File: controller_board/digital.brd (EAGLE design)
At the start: 148 x 129.2 mm, 34 parts

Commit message: Pull commit
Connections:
- removed net ENABLE_GATE: U$81.4
- net EN_GATE: now also U$81.4
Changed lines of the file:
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@@
 <wire x1="53.0225" y1="3.81" x2="53.0225" y2="5.715" width="0.6096" layer="1"/>
 <wire x1="53.0225" y1="5.715" x2="53.0225" y2="10.795" width="0.6096" layer="16"/>
+<contactref element="U$81" pad="4"/>
+<wire x1="55.245" y1="13.0175" x2="40.6375" y2="33.3675" width="0" layer="19" extent="1-16"/>
 </signal>
 <signal name="ADC_M1">
@@
 <wire x1="9.2075" y1="34.29" x2="6.6675" y2="34.29" width="1.016" layer="16"/>
 </signal>
-<signal name="ENABLE_GATE">
-<contactref element="U$81" pad="4"/>
-</signal>
 <signal name="-15V">

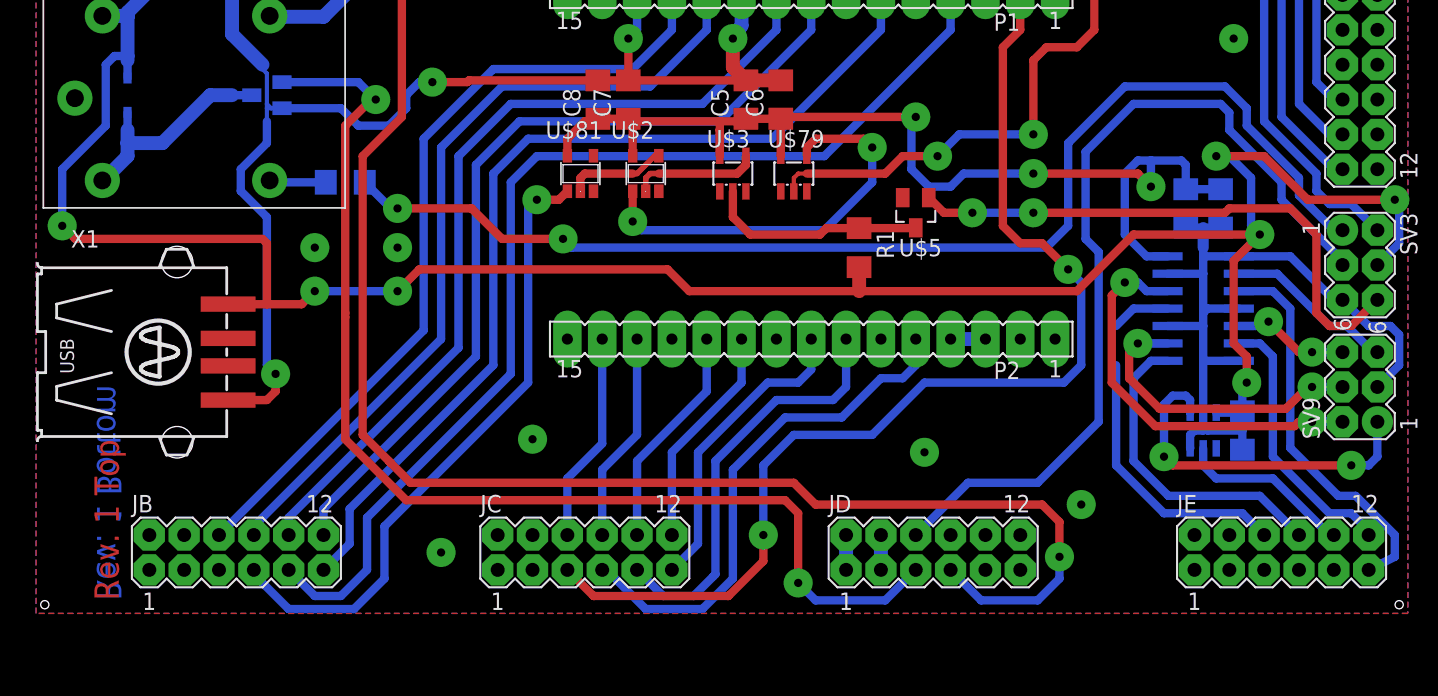
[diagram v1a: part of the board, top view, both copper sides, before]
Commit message: Added section of logic level shifters and drive enable signals!
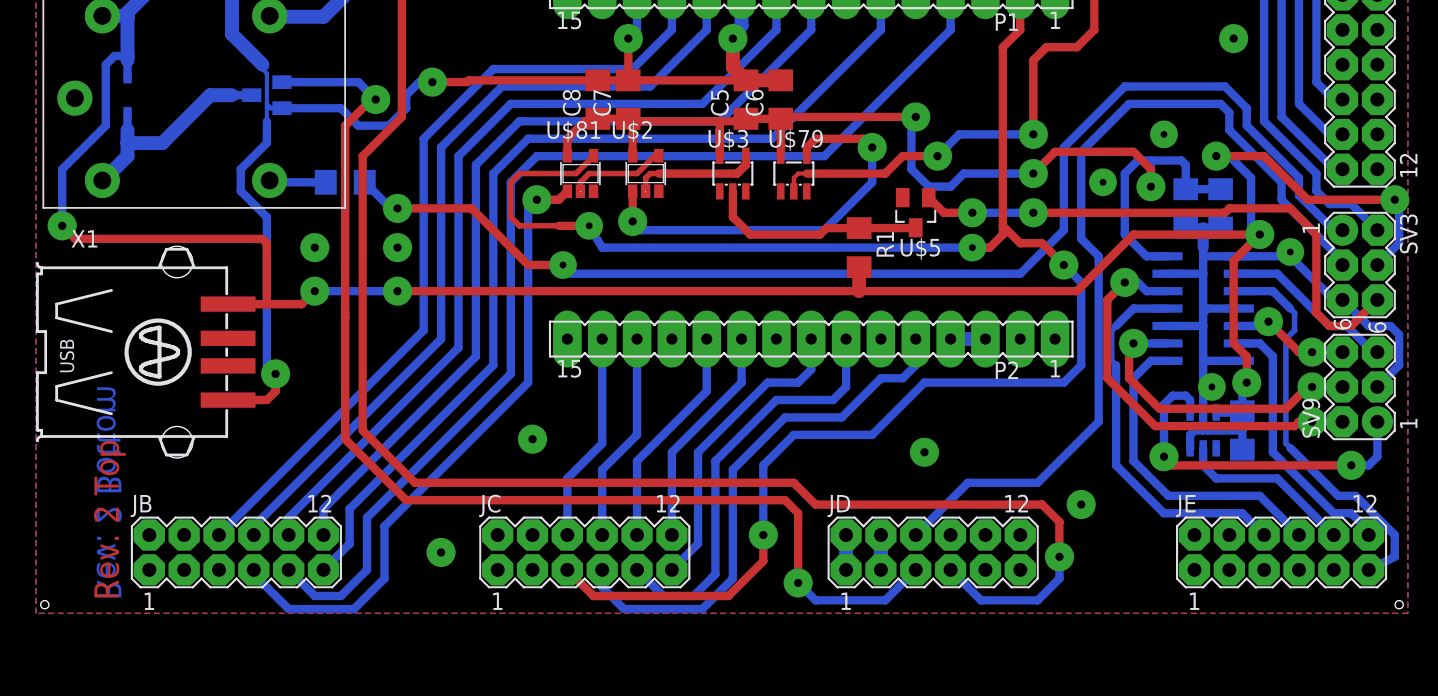
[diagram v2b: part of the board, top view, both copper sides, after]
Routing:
- net EN_GATE: track 80.4 -> 127.9 mm, vias 2 -> 4
- net +3V3: track 80.0 -> 82.0 mm
- net IR_RELAY: track 87.5 -> 89.1 mm
- net +5V: track 186.1 -> 184.8 mm
- net PWRGD: track 38.0 -> 38.7 mm
- net ZYBO_ENC_A: track 28.4 -> 28.9 mm
- net GNDD: vias 15 -> 19
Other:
- board text added: "Rev. 2 Bottom"
- board text added: "Rev. 2 Top"
- board text removed: "Rev. 1 Bottom"
- board text removed: "Rev. 1 Top"

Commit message: updates to boards
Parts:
- moved U$79 1.93 mm to (57.1, 32.4)
- moved R55 1.71 mm to (21.9, 33.0)
- moved U$3 0.71 mm to (51.1, 32.7)
- moved U$2 0.63 mm to (44.5, 32.7)
- moved U$81 0.63 mm to (39.7, 32.7)
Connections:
- removed net N$3: U$2.1, U$79.4
- removed net N$4: U$2.2, U$3.4
- new net ZYBO_OCP_EN_GATE: JB.5, U$2.1, U$79.4
- new net ZYBO_OTP_EN_GATE: JD.8, U$2.2, U$3.4
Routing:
- net GNDP: track 113.1 -> 7.79 mm
- net ZYBO_OCP_EN_GATE: track 0.00 -> 104.6 mm, vias 0 -> 5
- net ZYBO_OTP_EN_GATE: track 0.00 -> 69.2 mm, vias 0 -> 3
- net N$3: track 29.8 -> 0.00 mm, vias 2 -> 0
- net N$4: track 9.33 -> 0.00 mm
- net IR_RELAY: track 89.1 -> 92.1 mm
- net DRIVE_ENABLE: track 64.0 -> 66.8 mm
- net OCP_EN_GATE: track 66.6 -> 64.4 mm
- net ZYBO_IR_ENABLE: track 83.6 -> 85.4 mm
- net ZYBO_K1_ENABLE: track 121.6 -> 123.4 mm
- net ZYBO_EN_GATE: track 46.5 -> 47.5 mm
- net +3V3: track 82.0 -> 81.2 mm
- net EN_GATE: track 127.9 -> 128.8 mm
- net PWM2: track 59.7 -> 60.3 mm
- net GNDD: vias 19 -> 23
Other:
- board text added: "Rev. 3 Bottom"
- board text added: "Rev. 3 Top"
- board text removed: "Rev. 2 Bottom"
- board text removed: "Rev. 2 Top"

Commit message: Changes to Electronics Design
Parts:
- moved U$28 25.1 mm to (39.4, 54.0), flipped to the bottom, turned to 180 degrees
- moved U$46 11.4 mm to (13.0, 68.9), flipped to the bottom, turned to 180 degrees
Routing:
- net GNDD: track 200.3 -> 157.6 mm, vias 23 -> 22
- net GNDA: track 72.2 -> 32.4 mm
- net VBATT: track 92.4 -> 78.7 mm
- net +15V: track 21.9 -> 29.8 mm
- net -15V: track 29.1 -> 36.2 mm, vias 2 -> 1
- net +5V: track 185.1 -> 185.0 mm, vias 7 -> 8
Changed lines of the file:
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@@
 <attribute name="OC_NEWARK" value="unknown" x="96.52" y="16.51" size="1.778" layer="27" rot="R90" display="off"/>
 </element>
-<element name="U$28" library="custom_parts" package="TEN20-4823" value="TEN20-4823WIN" x="39.37" y="79.0575"/>
+<element name="U$28" library="custom_parts" package="TEN20-4823" value="TEN20-4823WIN" x="39.37" y="53.975" rot="MR180"/>
 <element name="U$36" library="custom_parts" package="SOT23-5L" value="SN74LVC1G17" x="85.09" y="13.335" rot="MR0"/>
-<element name="U$46" library="custom_parts" package="DIP24" value="TVN5-4811WI" x="13.0175" y="57.4675"/>
+<element name="U$46" library="custom_parts" package="DIP24" value="TVN5-4811WI" x="13.0175" y="68.8975" rot="MR180"/>
 <element name="U$49" library="custom_parts" package="JS1-5V-F" value="JS1-5V-F" x="11.43" y="37.465"/>
 <element name="U$55" library="custom_parts" package="MICROFIT-3.0" value="MICROFIT" x="29.21" y="76.835"/>
@@
 <wire x1="87.9475" y1="13.335" x2="85.4075" y2="13.335" width="0.6096" layer="16"/>
 <wire x1="85.4075" y1="13.335" x2="85.09" y2="13.6525" width="0.6096" layer="16"/>
-<wire x1="20.6375" y1="72.009" x2="17.7165" y2="72.009" width="1.016" layer="16"/>
-<wire x1="17.7165" y1="72.009" x2="16.51" y2="70.8025" width="1.016" layer="16"/>
-<wire x1="16.51" y1="70.8025" x2="16.51" y2="51.435" width="1.016" layer="16"/>
 <wire x1="15.5575" y1="46.355" x2="14.2875" y2="45.085" width="1.016" layer="16"/>
 <wire x1="14.2875" y1="45.085" x2="14.2875" y2="42.2275" width="1.016" layer="16"/>
@@
 <via x="66.675" y="13.0175" extent="1-16" drill="0.6"/>
 <contactref element="U$5" pad="2"/>
-<wire x1="5.3975" y1="51.816" x2="7.239" y2="51.816" width="1.016" layer="16"/>
-<wire x1="7.239" y1="51.816" x2="8.255" y2="51.7525" width="1.016" layer="16"/>
-<via x="8.255" y="51.7525" extent="1-16" drill="0.6"/>
-<wire x1="8.255" y1="51.7525" x2="13.0175" y2="51.7525" width="1.016" layer="1"/>
-<via x="13.0175" y="51.7525" extent="1-16" drill="0.6"/>
-<wire x1="13.0175" y1="51.7525" x2="16.1925" y2="51.7525" width="1.016" layer="16"/>
-<wire x1="16.1925" y1="51.7525" x2="16.51" y2="51.435" width="1.016" layer="16"/>
-<wire x1="16.51" y1="51.435" x2="16.51" y2="50.4825" width="1.016" layer="16"/>
-<wire x1="16.51" y1="50.4825" x2="17.78" y2="49.2125" width="1.016" layer="16"/>
-<wire x1="17.78" y1="49.2125" x2="20.574" y2="49.2125" width="1.016" layer="16"/>
-<wire x1="20.574" y1="49.2125" x2="20.6375" y2="49.149" width="1.016" layer="16"/>
 <wire x1="15.5575" y1="46.355" x2="19.685" y2="46.355" width="1.016" layer="16"/>
 <wire x1="19.685" y1="46.355" x2="20.6375" y2="47.3075" width="1.016" layer="16"/>
-<wire x1="20.6375" y1="47.3075" x2="20.6375" y2="49.149" width="1.016" layer="16"/>
 <wire x1="22.225" y1="36.83" x2="23.495" y2="35.56" width="0.6096" layer="16"/>
 <wire x1="23.495" y1="35.56" x2="25.7175" y2="35.56" width="0.6096" layer="16"/>
@@
 <via x="48.26" y="30.7975" extent="1-16" drill="0.6"/>
 <via x="54.2925" y="31.115" extent="1-16" drill="0.6"/>
+<via x="20.6375" y="47.3075" extent="1-16" drill="0.6"/>
+<wire x1="5.3975" y1="74.549" x2="20.6375" y2="77.216" width="0" layer="19" extent="1-1"/>
+<wire x1="20.6375" y1="54.356" x2="20.6375" y2="77.216" width="0" layer="19" extent="1-1"/>
 </signal>
 <signal name="ADC_M2">
@@
 <vertex x="87.3125" y="60.6425"/>
 </polygon>
-<wire x1="95.25" y1="67.6275" x2="82.55" y2="67.6275" width="1.016" layer="16"/>
-<wire x1="82.55" y1="67.6275" x2="76.2" y2="67.6275" width="1.016" layer="16"/>
-<wire x1="76.2" y1="67.6275" x2="74.93" y2="66.3575" width="1.016" layer="16"/>
-<wire x1="95.25" y1="75.2475" x2="84.7725" y2="75.2475" width="1.016" layer="16"/>
-<wire x1="84.7725" y1="75.2475" x2="82.55" y2="73.025" width="1.016" layer="16"/>
-<wire x1="82.55" y1="73.025" x2="82.55" y2="67.6275" width="1.016" layer="16"/>
 </signal>
 <signal name="VBATT">
@@
 <contactref element="U$46" pad="P$1"/>
 <contactref element="U$46" pad="P$2"/>
+<wire x1="38.735" y1="45.4025" x2="31.4325" y2="45.4025" width="1.016" layer="16"/>
 <wire x1="31.4325" y1="45.4025" x2="22.86" y2="45.4025" width="1.016" layer="16"/>
 <wire x1="22.86" y1="45.4025" x2="20.955" y2="43.4975" width="1.016" layer="16"/>
 <wire x1="20.955" y1="43.4975" x2="17.0975" y2="43.4975" width="1.016" layer="16"/>
 <wire x1="17.0975" y1="43.4975" x2="17.03" y2="43.565" width="1.016" layer="16"/>
-<wire x1="20.6375" y1="77.089" x2="20.6375" y2="74.549" width="1.016" layer="16"/>
-<wire x1="38.735" y1="45.4025" x2="31.4325" y2="45.4025" width="1.016" layer="16"/>
-<wire x1="31.4325" y1="72.7075" x2="31.4325" y2="68.8975" width="1.016" layer="16"/>
-<wire x1="31.4325" y1="68.8975" x2="31.4325" y2="45.4025" width="1.016" layer="16"/>
-<wire x1="54.61" y1="68.8975" x2="31.4325" y2="68.8975" width="1.016" layer="16"/>
-<wire x1="20.6375" y1="74.549" x2="21.336" y2="74.549" width="1.016" layer="16"/>
-<wire x1="21.336" y1="74.549" x2="22.86" y2="73.025" width="1.016" layer="16"/>
-<wire x1="22.86" y1="73.025" x2="31.115" y2="73.025" width="1.016" layer="16"/>
 <wire x1="31.115" y1="73.025" x2="31.4325" y2="72.7075" width="1.016" layer="16"/>
 <wire x1="31.4325" y1="72.7075" x2="31.4325" y2="73.9775" width="1.016" layer="16"/>
 <wire x1="31.4325" y1="73.9775" x2="32.7025" y2="75.2475" width="1.016" layer="16"/>
 <wire x1="32.7025" y1="75.2475" x2="32.7025" y2="77.47" width="1.016" layer="16"/>
+<wire x1="31.4325" y1="72.7075" x2="31.4325" y2="64.135" width="1.016" layer="16"/>
+<wire x1="31.4325" y1="64.135" x2="31.4325" y2="45.4025" width="1.016" layer="16"/>
+<wire x1="54.61" y1="64.135" x2="31.4325" y2="64.135" width="1.016" layer="16"/>
+<wire x1="20.6375" y1="49.276" x2="20.6375" y2="51.816" width="0" layer="19" extent="1-1"/>
+<wire x1="22.86" y1="45.4025" x2="20.6375" y2="49.276" width="0" layer="19" extent="16-16"/>
 </signal>
 <signal name="GNDP">
@@
 <wire x1="41.275" y1="45.4025" x2="41.2775" y2="45.4025" width="1.016" layer="16"/>
 <wire x1="41.2775" y1="45.4025" x2="41.2775" y2="53.1925" width="1.27" layer="16"/>
+<wire x1="5.3975" y1="49.149" x2="5.3975" y2="51.689" width="0" layer="19" extent="1-1"/>
+<wire x1="29.68625" y1="77.47" x2="5.3975" y2="51.689" width="0" layer="19" extent="1-1"/>
 </signal>
 <signal name="DRIVE_ENABLE">
@@
 <contactref element="U$28" pad="P$5"/>
 <contactref element="D/A1" pad="18"/>
-<wire x1="95.25" y1="70.1675" x2="92.075" y2="70.1675" width="1.016" layer="16"/>
-<via x="92.075" y="70.1675" extent="1-16" drill="0.6"/>
-<wire x1="92.075" y1="70.1675" x2="83.82" y2="70.1675" width="1.016" layer="1"/>
-<wire x1="83.82" y1="70.1675" x2="74.93" y2="61.2775" width="1.016" layer="1"/>
 <via x="74.93" y="61.2775" extent="1-16" drill="0.6"/>
-<wire x1="74.93" y1="61.2775" x2="74.93" y2="56.1975" width="1.016" layer="16"/>
+<wire x1="95.25" y1="70.1675" x2="81.5975" y2="70.1675" width="1.016" layer="16"/>
+<wire x1="81.5975" y1="70.1675" x2="74.93" y2="76.835" width="1.016" layer="16"/>
+<wire x1="74.93" y1="61.2775" x2="77.47" y2="61.2775" width="1.016" layer="16"/>
+<wire x1="77.47" y1="61.2775" x2="81.5975" y2="65.405" width="1.016" layer="16"/>
+<wire x1="81.5975" y1="65.405" x2="81.5975" y2="70.1675" width="1.016" layer="16"/>
 </signal>
 <signal name="N$42">
@@
 <wire x1="14" y1="22.55" x2="15.2325" y2="22.55" width="1.016" layer="1"/>
 <wire x1="15.2325" y1="22.55" x2="15.24" y2="22.5425" width="1.016" layer="1"/>
-<wire x1="5.461" y1="56.8325" x2="5.3975" y2="56.896" width="1.016" layer="16"/>
+<wire x1="5.461" y1="56.8325" x2="5.3975" y2="69.469" width="0" layer="19" extent="1-16"/>
 <wire x1="8.255" y1="56.8325" x2="5.461" y2="56.8325" width="1.016" layer="16"/>
 <wire x1="88.265" y1="16.8275" x2="88.265" y2="18.7325" width="0.6096" layer="1"/>
@@
 <wire x1="18.415" y1="23.1775" x2="17.145" y2="23.1775" width="0.6096" layer="1"/>
 <wire x1="17.145" y1="23.1775" x2="16.8275" y2="22.86" width="0.6096" layer="1"/>
+<via x="5.461" y="56.8325" extent="1-16" drill="0.6"/>
 </signal>
 <signal name="N$5">
@@
 <wire x1="95.25" y1="72.7075" x2="92.075" y2="72.7075" width="1.016" layer="16"/>
 <via x="92.075" y="72.7075" extent="1-16" drill="0.6"/>
-<wire x1="92.075" y1="72.7075" x2="82.8675" y2="72.7075" width="1.016" layer="1"/>
-<wire x1="82.8675" y1="72.7075" x2="79.0575" y2="76.5175" width="1.016" layer="1"/>
-<via x="79.0575" y="76.5175" extent="1-16" drill="0.6"/>
-<wire x1="79.0575" y1="76.5175" x2="74.93" y2="76.5175" width="1.016" layer="16"/>
+<wire x1="88.5825" y1="67.945" x2="77.1525" y2="56.515" width="1.016" layer="16"/>
+<wire x1="77.1525" y1="56.515" x2="74.93" y2="56.515" width="1.016" layer="16"/>
+<wire x1="92.075" y1="72.7075" x2="92.075" y2="67.945" width="1.016" layer="1"/>
+<via x="92.075" y="67.945" extent="1-16" drill="0.6"/>
+<wire x1="92.075" y1="67.945" x2="88.5825" y2="67.945" width="1.016" layer="16"/>
 </signal>
 <signal name="OTP_EN_GATE">
